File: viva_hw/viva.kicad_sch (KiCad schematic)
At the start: 16 parts, among them M1 Motor_DC, M2 Motor_DC, M3 Motor_DC, M4 Motor_DC, Q1 2N3904, Q2 2N3904, Q3 2N3904, Q4 2N3904, U1 XIAO ESP32C3

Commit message: feat: updated footprints
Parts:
- removed M1, M2, M3, M4: Motor_DC, symbol Motor:Motor_DC
- removed U1: XIAO ESP32C3, RF_Module:MCU_Seeed_ESP32C3, symbol xiao_esp32c3:XIAO ESP32C3
- added J1: Conn_01x05_Socket, Connector_PinHeader_2.54mm:PinHeader_1x05_P2.54mm_Vertical, symbol Connector:Conn_01x05_Socket
- added M1: XIAO_ESP32C3, System_On_Chip:XIAO_ESP32C3_THR, symbol System_On_Chip:XIAO_ESP32C3
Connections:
- net 0: now also M1.13 (GND)
- net EMG: now also M1.2 (D1)
- net VCC: now also J1.1 (Pin_1), M1.12 (3v3)
- net at D3.2 (A), Q3.3 (C): now also J1.3 (Pin_3)
- net at D4.2 (A), Q4.3 (C): now also J1.2 (Pin_2)
- net at D2.2 (A), Q2.3 (C): now also J1.4 (Pin_4)
- net at Q3.2 (B): now also M1.6 (D5)
- net at Q2.2 (B): now also M1.5 (D4)
- net at R3.1, R4.1: now also M1.1 (D0)
- net at R3.2: now also M1.16 (BAT+)
- net at R4.2: now also M1.15 (BAT-)
- net at ST7735.4 (Pin_4): now also M1.10 (D9)
- net at ST7735.3 (Pin_3): now also M1.11 (D10)
- net at ST7735.5 (Pin_5): now also M1.3 (D2)
- net at Q1.2 (B): now also M1.4 (D3)
- net at Q4.2 (B): now also M1.7 (D6)
- net at ST7735.7 (Pin_7): now also M1.8 (D7)
- net at ST7735.6 (Pin_6): now also M1.9 (D8)
- net at D1.2 (A), Q1.3 (C): now also J1.5 (Pin_5)
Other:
- moved on the sheet: Q2

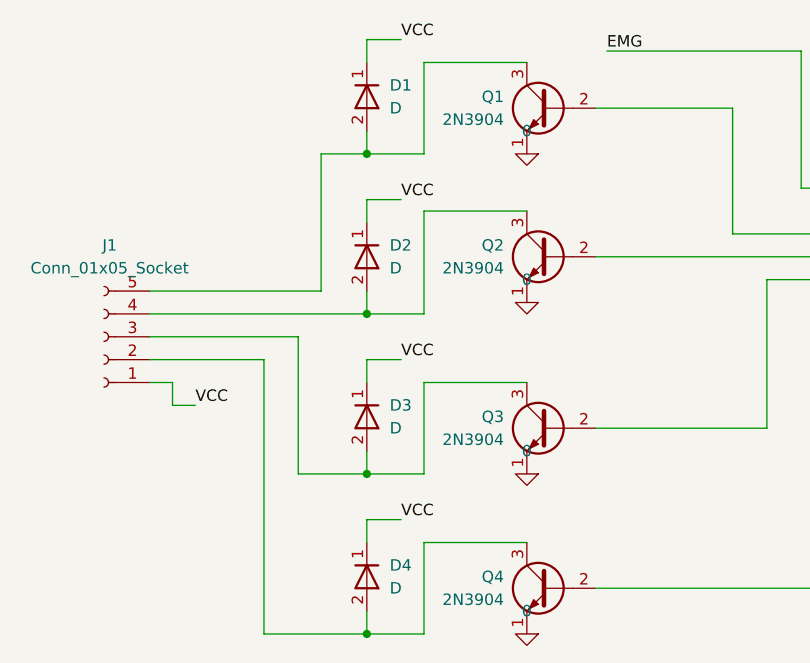
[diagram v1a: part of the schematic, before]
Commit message: feat: changed socket size for display
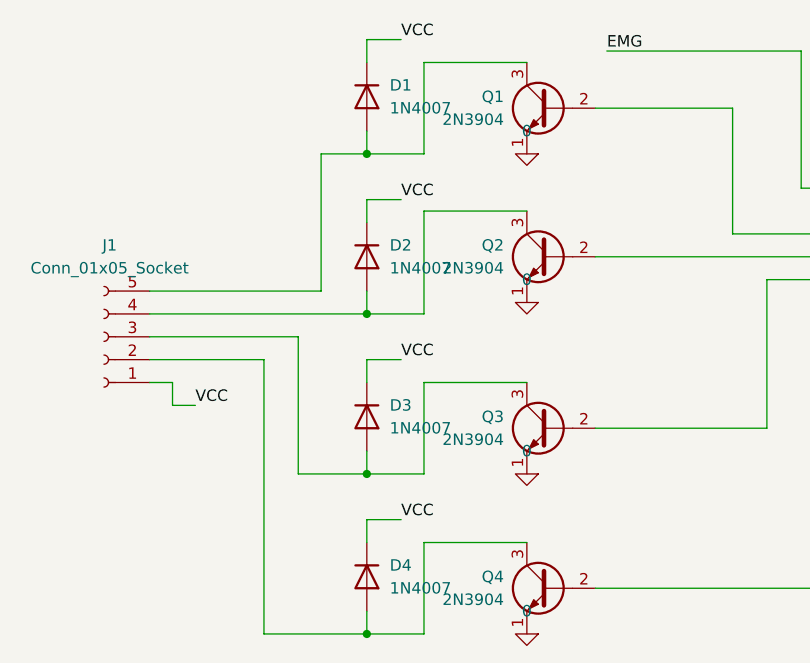
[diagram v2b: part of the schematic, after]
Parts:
- removed D1, D2, D3, D4: D, symbol Simulation_SPICE:D
- added D1, D2, D3, D4: 1N4007, Diode_THT:D_DO-41_SOD81_P10.16mm_Horizontal, symbol Diode:1N4007
- ST7735: footprint Connector_PinHeader_1.00mm:PinHeader_1x08_P1.00mm_Vertical -> Connector_PinHeader_2.54mm:PinHeader_1x08_P2.54mm_Vertical
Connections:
- net VCC: now also D1.1 (K), D2.1 (K), D3.1 (K), D4.1 (K)
- net at J1.3 (Pin_3), Q3.3 (C): now also D3.2 (A)
- net at J1.2 (Pin_2), Q4.3 (C): now also D4.2 (A)
- net at J1.4 (Pin_4), Q2.3 (C): now also D2.2 (A)
- net at J1.5 (Pin_5), Q1.3 (C): now also D1.2 (A)

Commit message: feat: began emg work
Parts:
- added U1, U2: TL072, Package_DIP:CERDIP-8_W7.62mm_SideBrazed_Socket, symbol Amplifier_Operational:TL072
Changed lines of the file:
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@@
+	)
+	(symbol
+		(lib_id "Amplifier_Operational:TL072")
+		(at 45.72 44.45 0)
+		(unit 1)
+		(exclude_from_sim no)
+		(in_bom yes)
+		(on_board yes)
+		(dnp no)
+		(fields_autoplaced yes)
+		(property "Reference" "U1"
+			(at 45.72 34.29 0)
+			(effects
+				(font
+					(size 1.27 1.27)
+				)
+			)
+		)
+		(property "Value" "TL072"
+			(at 45.72 36.83 0)
+			(effects
+				(font
+					(size 1.27 1.27)
+				)
+			)
+		)
+		(property "Footprint" "Package_DIP:CERDIP-8_W7.62mm_SideBrazed_Socket"
+			(at 45.72 44.45 0)
+			(effects
+				(font
+					(size 1.27 1.27)
+				)
+				(hide yes)
+			)
+		)
+		(property "Datasheet" "http://www.ti.com/lit/ds/symlink/tl071.pdf"
+			(at 45.72 44.45 0)
+			(effects
+				(font
+					(size 1.27 1.27)
+				)
+				(hide yes)
+			)
+		)
+		(property "Description" "Dual Low-Noise JFET-Input Operational Amplifiers, DIP-8/SOIC-8"
+			(at 45.72 44.45 0)
+			(effects
+				(font
+					(size 1.27 1.27)
+				)
+				(hide yes)
+			)
+		)
+		(pin "5"
+		)
+		(pin "6"
+		)
+		(pin "7"
+		)
+		(pin "8"
+		)
+		(pin "1"
+		)
+		(pin "3"
+		)
+		(pin "2"
+		)
+		(pin "4"
+		)
+		(instances
+			(project ""
+				(path "/84312fb1-9f98-4e67-94cf-324cfeff20d6"
+					(reference "U1")
+					(unit 1)
+				)
+			)
+		)
 	)
 	(symbol
@@
 	)
 	(symbol
+		(lib_id "Amplifier_Operational:TL072")
+		(at 90.17 44.45 0)
+		(unit 3)
+		(exclude_from_sim no)
+		(in_bom yes)
+		(on_board yes)
+		(dnp no)
+		(fields_autoplaced yes)
+		(property "Reference" "U1"
+			(at 90.17 34.29 0)
+			(effects
+				(font
+					(size 1.27 1.27)
+				)
+			)
+		)
+		(property "Value" "TL072"
+			(at 90.17 36.83 0)
+			(effects
+				(font
+					(size 1.27 1.27)
+				)
+			)
+		)
+		(property "Footprint" "Package_DIP:CERDIP-8_W7.62mm_SideBrazed_Socket"
+			(at 90.17 44.45 0)
+			(effects
+				(font
+					(size 1.27 1.27)
+				)
+				(hide yes)
+			)
+		)
+		(property "Datasheet" "http://www.ti.com/lit/ds/symlink/tl071.pdf"
+			(at 90.17 44.45 0)
+			(effects
+				(font
+					(size 1.27 1.27)
+				)
+				(hide yes)
+			)
+		)
+		(property "Description" "Dual Low-Noise JFET-Input Operational Amplifiers, DIP-8/SOIC-8"
+			(at 90.17 44.45 0)
+			(effects
+				(font
+					(size 1.27 1.27)
+				)
+				(hide yes)
+			)
+		)
+		(pin "5"
+		)
+		(pin "6"
+		)
+		(pin "7"
+		)
+		(pin "8"
+		)
+		(pin "1"
+		)
+		(pin "3"
+		)
+		(pin "2"
+		)
+		(pin "4"
+		)
+		(instances
+			(project "viva"
+				(path "/84312fb1-9f98-4e67-94cf-324cfeff20d6"
+					(reference "U1")
+					(unit 3)
+				)
+			)
+		)
+	)
+	(symbol
 		(lib_id "Diode:1N4007")
 		(at 69.85 123.19 270)
@@
 				)
 			)
+		)
+	)
+	(symbol
+		(lib_id "Amplifier_Operational:TL072")
+		(at 69.85 44.45 0)
+		(unit 2)
+		(exclude_from_sim no)
+		(in_bom yes)
+		(on_board yes)
+		(dnp no)
+		(fields_autoplaced yes)
+		(property "Reference" "U2"
+			(at 69.85 34.29 0)
+			(effects
+				(font
+					(size 1.27 1.27)
+				)
+			)
+		)
+		(property "Value" "TL072"
+			(at 69.85 36.83 0)
+			(effects
+				(font
+					(size 1.27 1.27)
+				)
+			)
+		)
+		(property "Footprint" "Package_DIP:CERDIP-8_W7.62mm_SideBrazed_Socket"
+			(at 69.85 44.45 0)
+			(effects
+				(font
+					(size 1.27 1.27)
+				)
+				(hide yes)
+			)
+		)
+		(property "Datasheet" "http://www.ti.com/lit/ds/symlink/tl071.pdf"
+			(at 69.85 44.45 0)
+			(effects
+				(font
+					(size 1.27 1.27)
+				)
+				(hide yes)
+			)
+		)
+		(property "Description" "Dual Low-Noise JFET-Input Operational Amplifiers, DIP-8/SOIC-8"
+			(at 69.85 44.45 0)
+			(effects
+				(font
+					(size 1.27 1.27)
+				)
+				(hide yes)
+			)
+		)
+		(pin "5"
+		)
+		(pin "6"
+		)
+		(pin "7"
+		)
+		(pin "8"
+		)
+		(pin "1"
+		)
+		(pin "3"
+		)
+		(pin "2"
+		)
+		(pin "4"
+		)
+		(instances
+			(project "viva"
+				(path "/84312fb1-9f98-4e67-94cf-324cfeff20d6"
+					(reference "U2")
+					(unit 2)
+				)
+			)

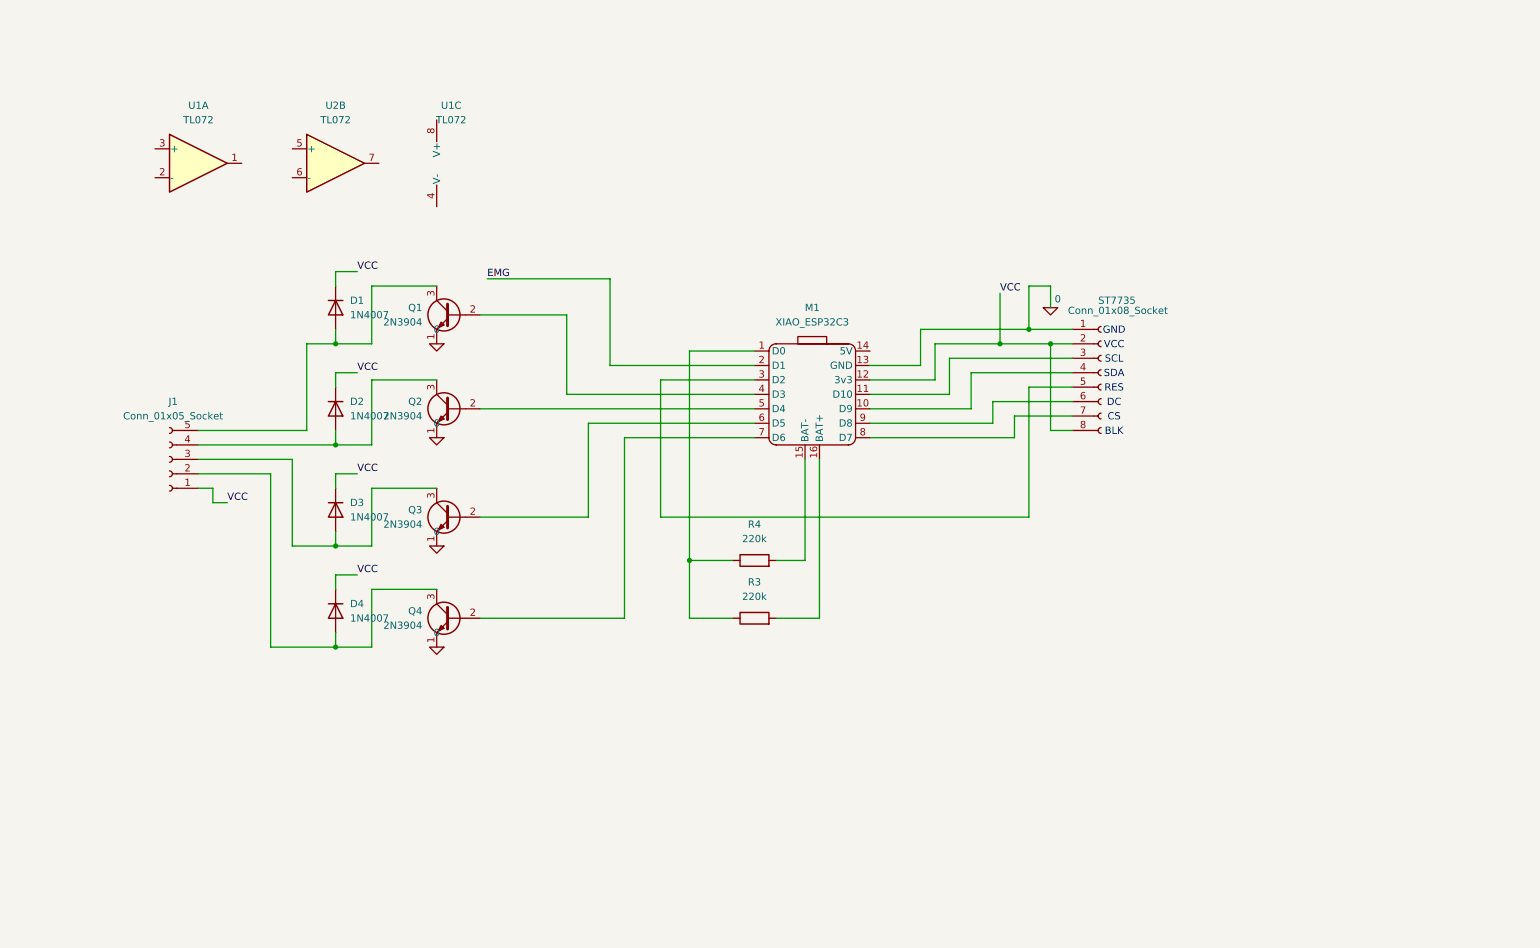
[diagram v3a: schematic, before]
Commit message: feat: added emg circuit
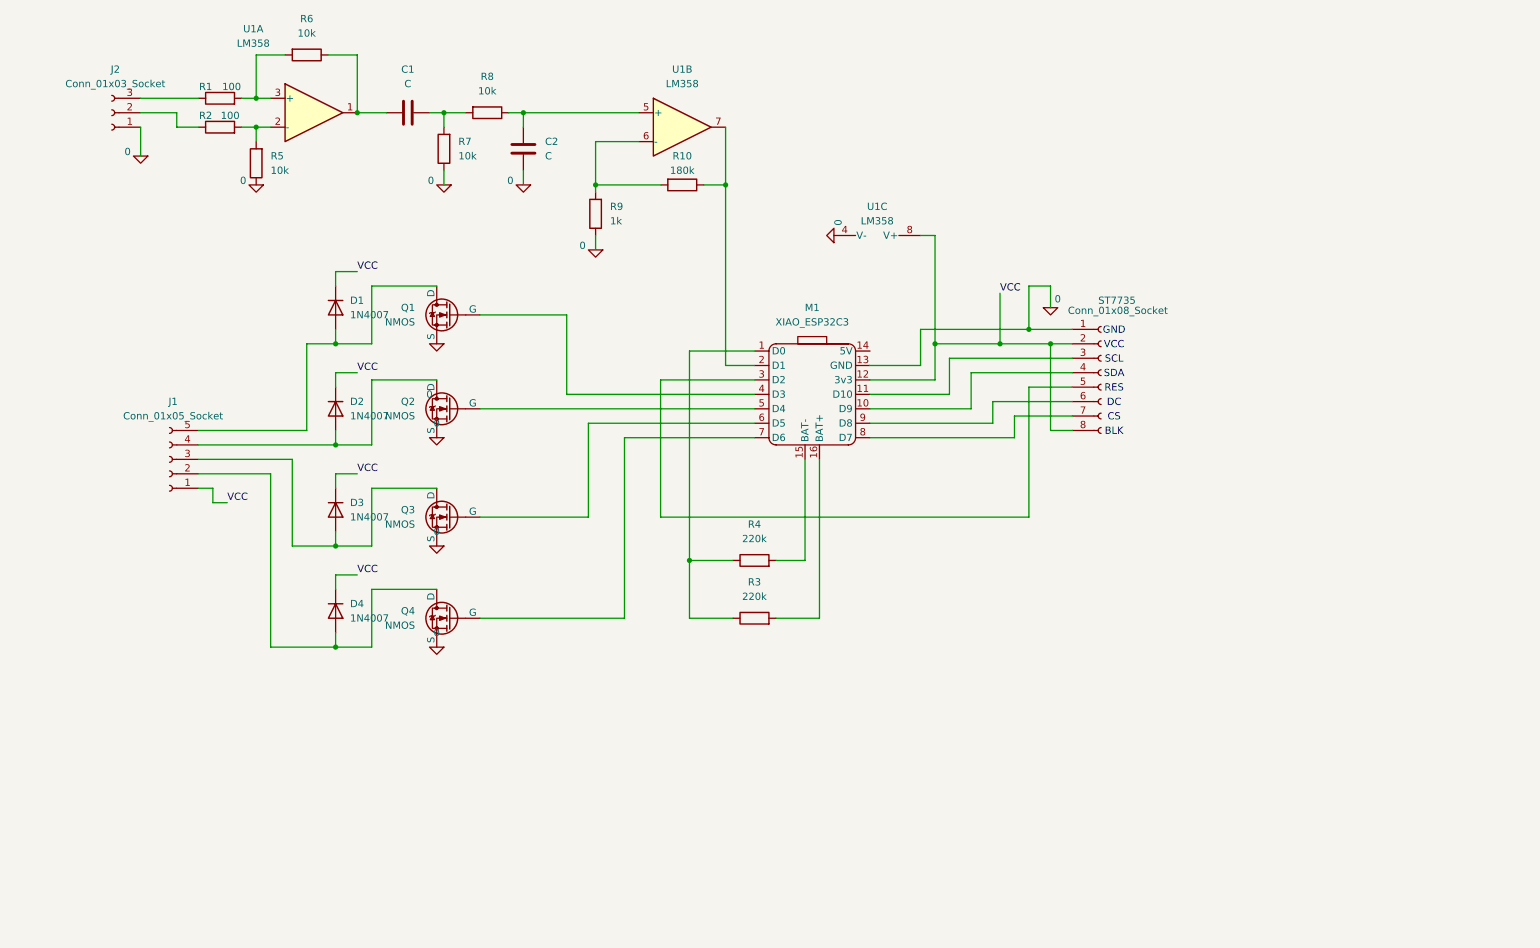
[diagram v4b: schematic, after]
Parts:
- removed Q1, Q2, Q3, Q4: 2N3904, Package_TO_SOT_THT:TO-92_Inline, symbol Transistor_BJT:2N3904
- removed U1, U2: TL072, Package_DIP:CERDIP-8_W7.62mm_SideBrazed_Socket, symbol Amplifier_Operational:TL072
- added C1, C2: C, symbol Device:C
- added J2: Conn_01x03_Socket, symbol Connector:Conn_01x03_Socket
- added Q1, Q2, Q3, Q4: NMOS, Package_TO_SOT_THT:TO-126-3_Vertical, symbol Simulation_SPICE:NMOS
- added R1, R2: 100, symbol Device:R
- added R10: 180k, symbol Device:R
- added R5, R6, R7, R8: 10k, symbol Device:R
- added R9: 1k, symbol Device:R
- added U1: LM358, Package_DIP:DIP-8_W7.62mm_Socket, symbol Amplifier_Operational:LM358
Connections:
- net 0: now also C2.1, J2.1 (Pin_1), Q1.3 (S), Q2.3 (S), Q3.3 (S), Q4.3 (S), R5.1, R7.1, R9.1, U1.4 (V-)
- net VCC: now also U1.8 (V+)
- net at M1.6 (D5): now also Q3.2 (G)
- net at D3.2 (A), J1.3 (Pin_3): now also Q3.1 (D)
- net at M1.5 (D4): now also Q2.2 (G)
- net at D2.2 (A), J1.4 (Pin_4): now also Q2.1 (D)
- net at D4.2 (A), J1.2 (Pin_2): now also Q4.1 (D)
- net at D1.2 (A), J1.5 (Pin_5): now also Q1.1 (D)
- net at M1.4 (D3): now also Q1.2 (G)
- net at M1.7 (D6): now also Q4.2 (G)
- net EMG: no longer names the net of M1.2 (D1)
- net EMG: now also R10.1, U1.7
- new net: C1.2, R7.2, R8.2
- new net: C1.1, R6.1, U1.1
- new net: R2.2, R5.2, U1.2 (-)
- new net: R1.2, R6.2, U1.3 (+)
- new net: C2.2, R8.1, U1.5 (+)
- new net: R10.2, R9.2, U1.6 (-)
- new net: J2.3 (Pin_3), R1.1
- new net: J2.2 (Pin_2), R2.1

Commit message: feat: backup
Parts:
- C1: value C -> 147n
- C2: value C -> 30n
- R7: value 10k -> 47k
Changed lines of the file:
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@@
 			)
 		)
-		(property "Value" "10k"
+		(property "Value" "47k"
 			(at 91.44 43.1799 0)
 			(effects
@@
 			)
 		)
-		(property "Value" "C"
+		(property "Value" "147n"
 			(at 82.55 30.48 90)
 			(effects
@@
 			)
 		)
-		(property "Value" "C"
+		(property "Value" "30n"
 			(at 106.68 43.1799 0)
 			(effects

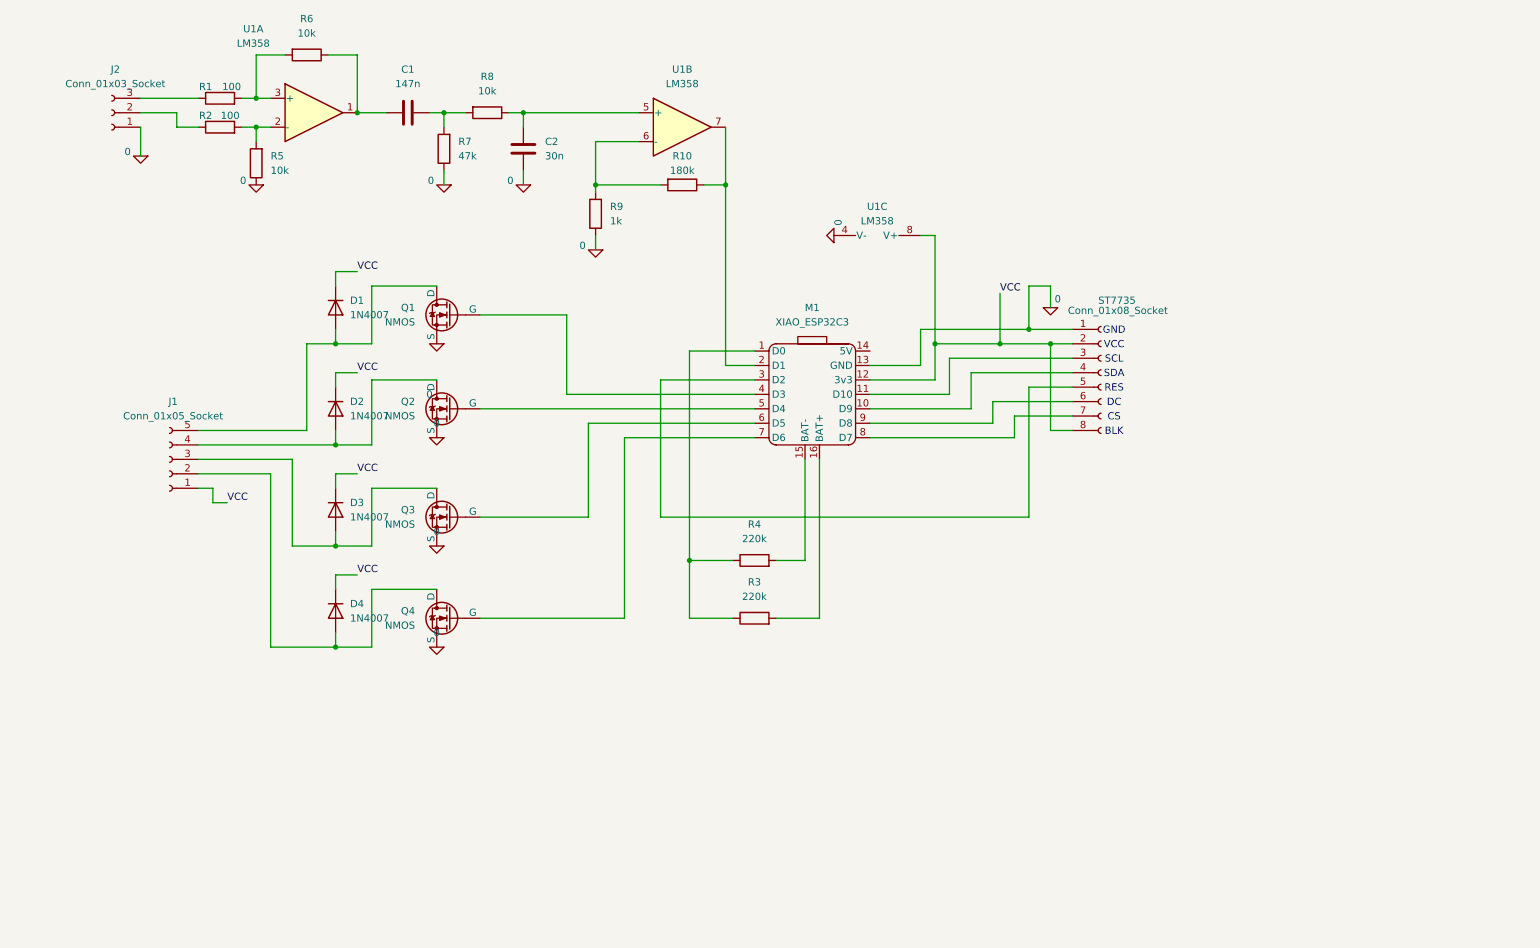
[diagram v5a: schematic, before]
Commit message: feat: added sallen key filters
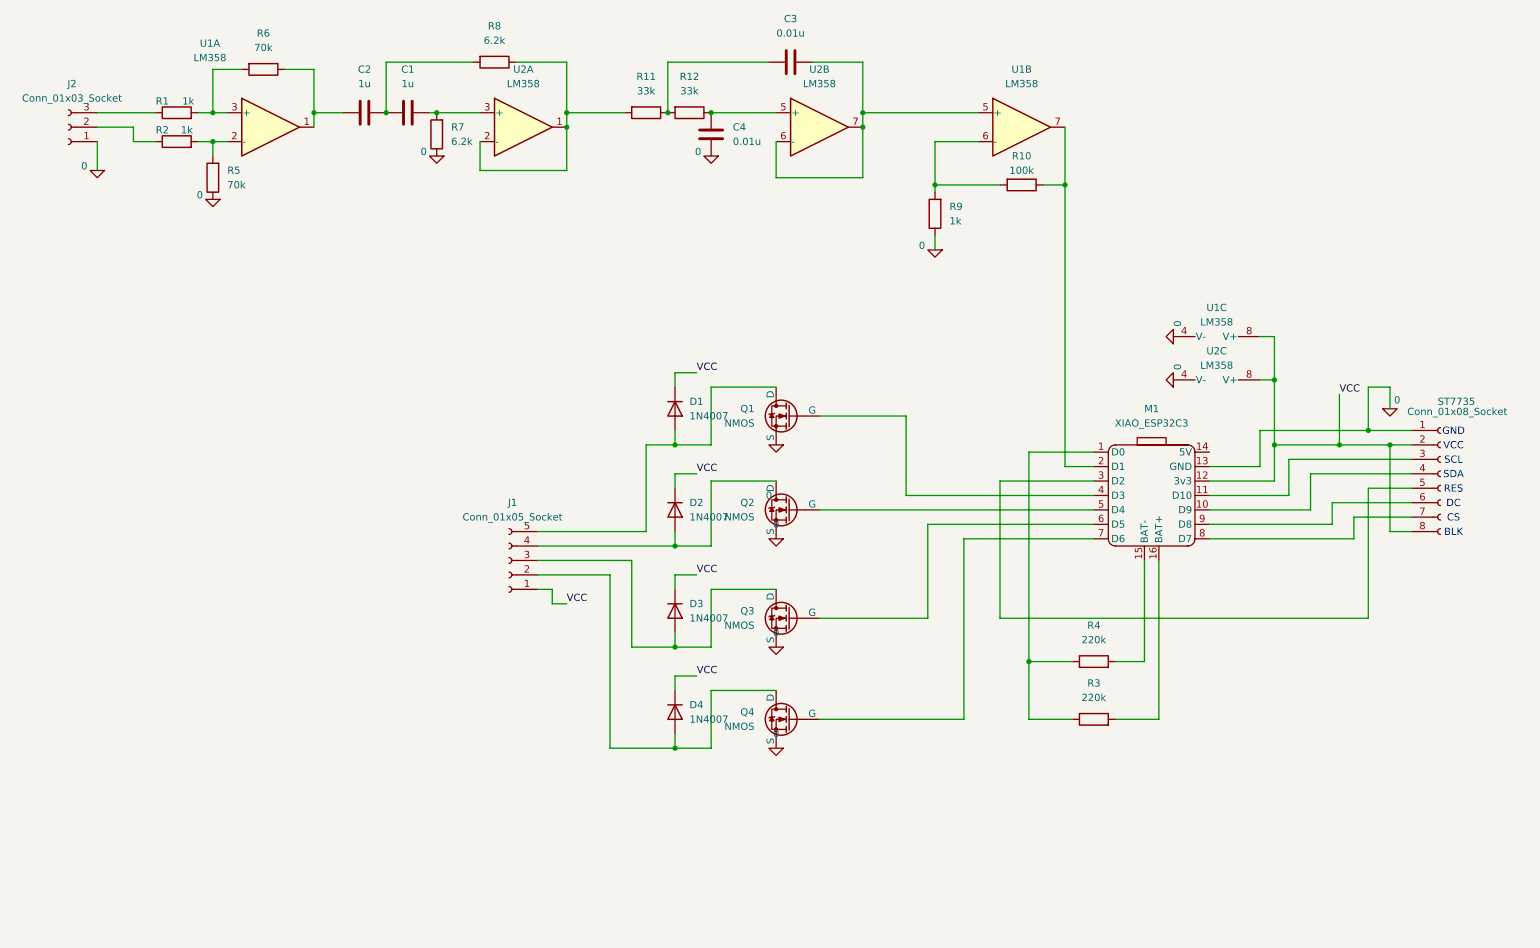
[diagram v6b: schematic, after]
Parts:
- added C3, C4: 0.01u, symbol Device:C
- added R11, R12: 33k, symbol Device:R
- added U2: LM358, symbol Amplifier_Operational:LM358
- C1: value 147n -> 1u
- C2: value 30n -> 1u
- R1, R2: value 100 -> 1k
- R10: value 180k -> 100k
- R5, R6: value 10k -> 70k
- R7: value 47k -> 6.2k
- R8: value 10k -> 6.2k
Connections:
- net 0: now also C4.1, U2.4 (V-); no longer C2.1
- net VCC: now also U2.8 (V+)
- net at C1.2, R7.2: now also U2.3 (+); no longer R8.2
- net at R6.1, U1.1: now also C2.1; no longer C1.1
- new net: C4.2, R12.1, U2.5 (+)
- new net: C3.1, R11.1, R12.2
- new net: R11.2, R8.1, U2.1, U2.2 (-)
- new net: C1.1, C2.2, R8.2
- new net: C3.2, U1.5 (+), U2.6 (-), U2.7
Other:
- moved on the sheet: D1, D2, D3, D4, J1, J2, M1, Q1, Q2, Q3, Q4, R1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
